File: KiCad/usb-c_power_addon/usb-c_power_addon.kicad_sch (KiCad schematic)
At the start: 22 parts, among them J1 GT-USB-7025, J10 10PIN_HEADER, J11 10PIN_HEADER, J15 12PIN_SERVO_HEADER, J3 1987724, J4 1987724, J5 1987724, J6 1987724, J7 3PIN_HEADER, J8 15PIN_HEADER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

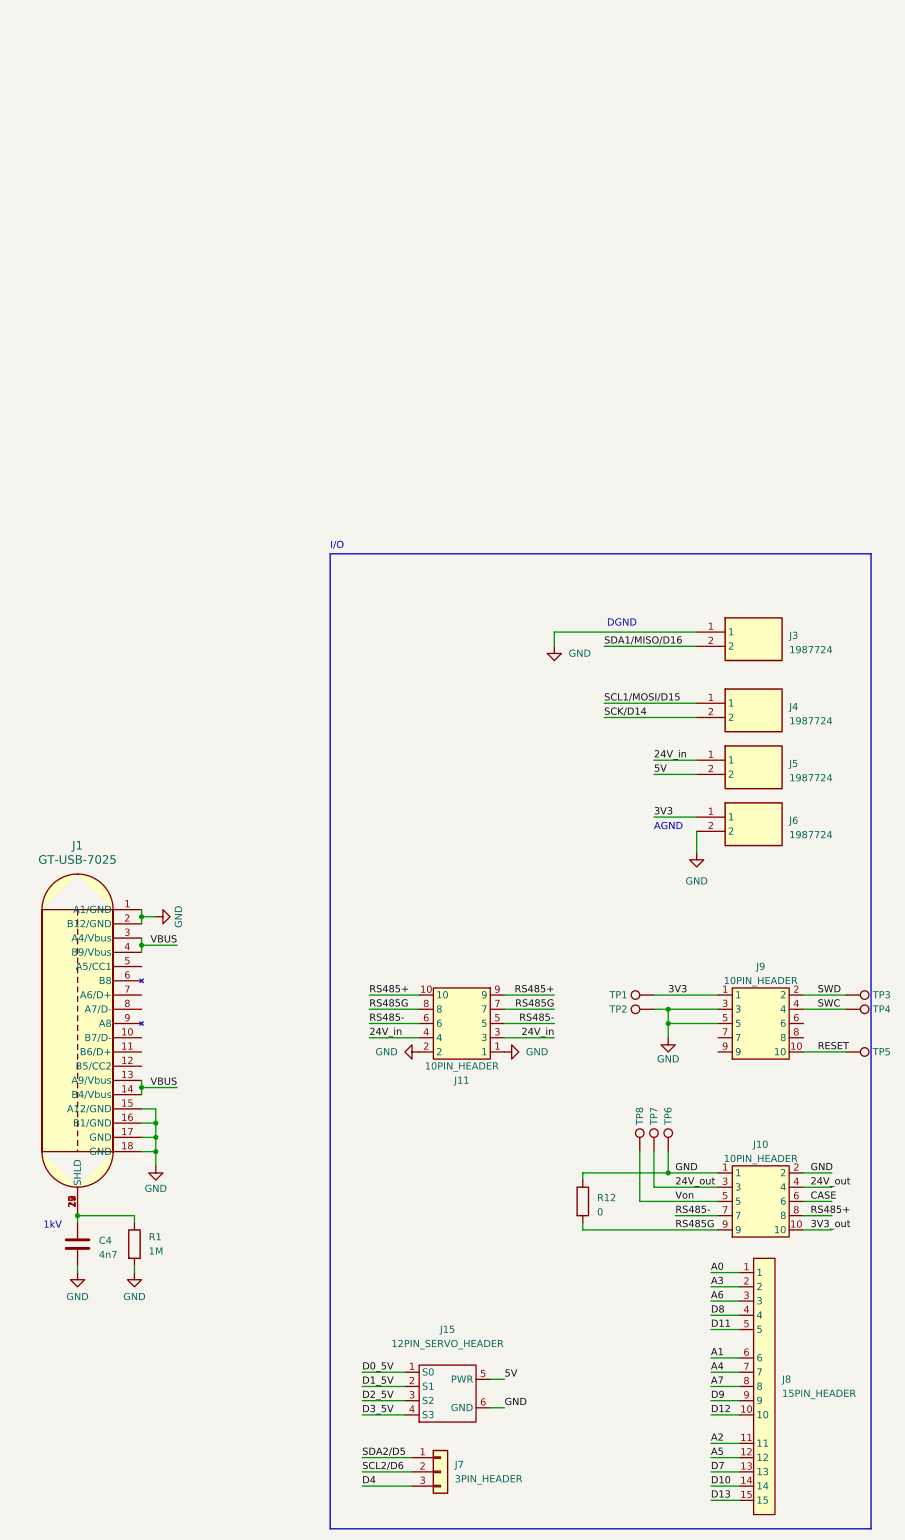
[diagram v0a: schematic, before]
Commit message: finished usb-c power addon, fixed main usbc wonky traces
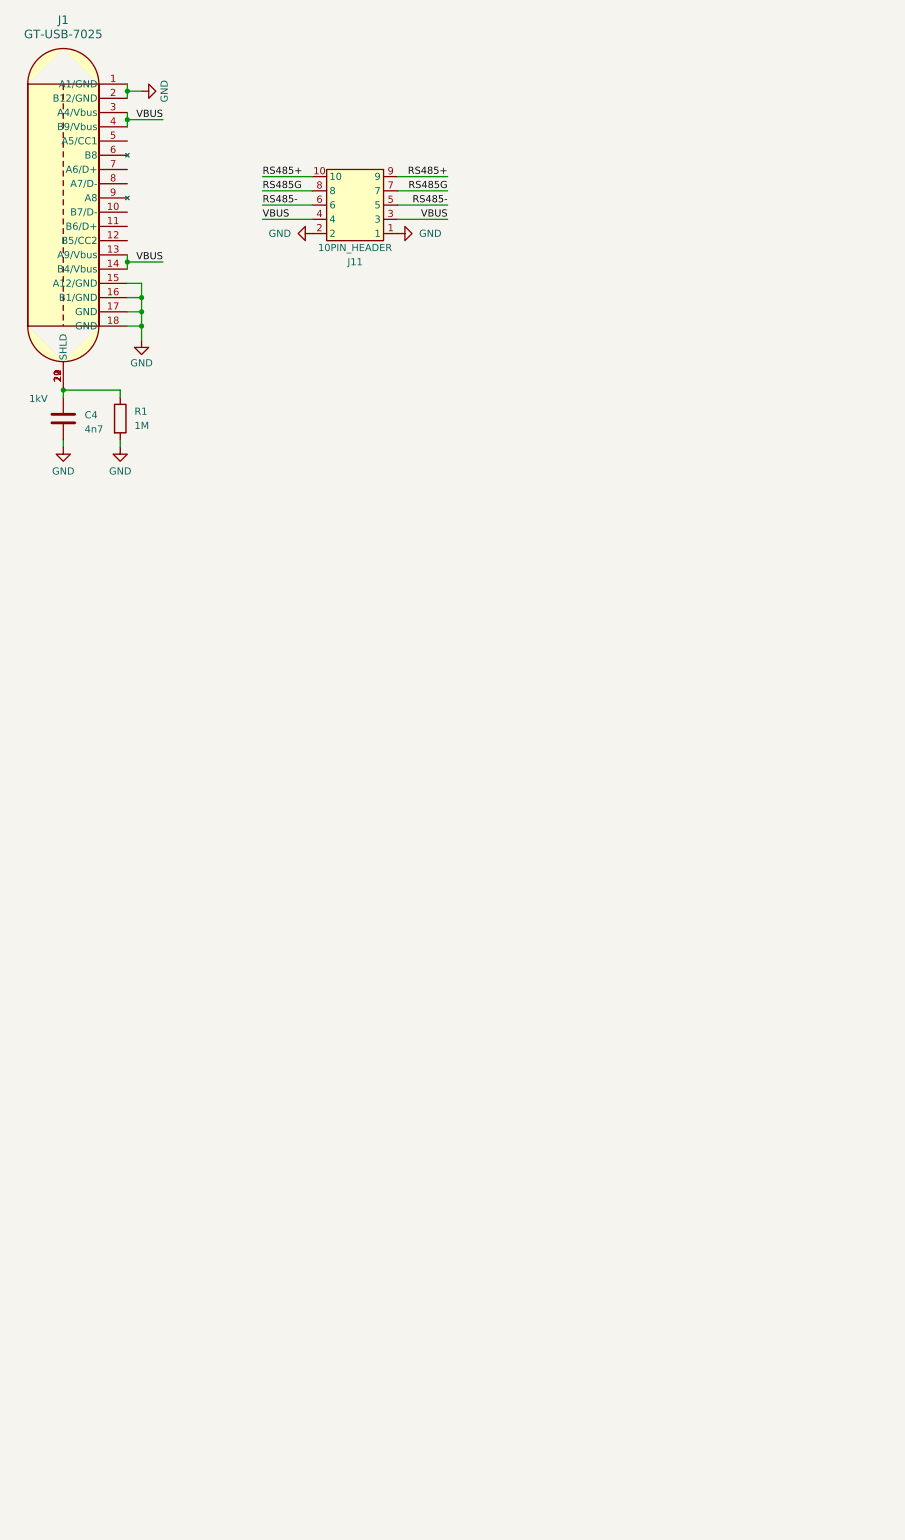
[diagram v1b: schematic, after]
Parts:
- removed J10: 10PIN_HEADER, robotiq_wrist_coupling:10PIN_SPRING_HEADER, symbol robotiq_wrist_coupling:10PIN_HEADER
- removed J15: 12PIN_SERVO_HEADER, robotiq_wrist_coupling:12PIN_SERVO_HEADER, symbol robotiq_wrist_coupling:12PIN_SERVO_HEADER
- removed J3, J4, J5, J6: 1987724, robotiq_wrist_coupling:1987724, symbol robotiq_wrist_coupling:1987724
- removed J7: 3PIN_HEADER, Connector_PinSocket_2.54mm:PinSocket_1x03_P2.54mm_Vertical, symbol Connector_Generic:Conn_01x03
- removed J8: 15PIN_HEADER, robotiq_wrist_coupling:15PIN_HEADER, symbol robotiq_wrist_coupling:15PIN_HEADER
- removed J9: 10PIN_HEADER, robotiq_wrist_coupling:10PIN_1.27PITCH, symbol robotiq_wrist_coupling:10PIN_HEADER
- removed R12: 0, Resistor_SMD:R_0603_1608Metric, symbol Device:R
- removed TP1, TP2, TP3, TP4, TP5: TestPoint, TestPoint:TestPoint_Pad_D1.5mm, symbol Connector:TestPoint
- removed TP6, TP7, TP8: TestPoint, TestPoint:TestPoint_THTPad_D1.5mm_Drill0.7mm, symbol Connector:TestPoint
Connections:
- net 24V_in is gone; now on net VBUS: J11.3, J11.4
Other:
- note removed: "AGND"
- note removed: "DGND"
- note removed: "I/O"
- moved on the sheet: C4, J1, J11, R1
